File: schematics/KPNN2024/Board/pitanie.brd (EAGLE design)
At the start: 68.9 x 68.2 mm, 42 parts, among them X1 JST-2-2.5, X2 JST-2-2.5

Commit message: Платы вроде готовы
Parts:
- added 3V3, 5V: (no value), led:CHIP-LED0603
- added R11, R12: 2k, rcl:R0603
- MP1584-5V: value MP1584-B -> MP1584
- U$14: value MOLEX-4-1.25 -> BLUETOOTH
- U$9: value JST-4-2.5 -> STEP_MOT
- X1: value JST-2-2.5 -> PERE
- X2: value JST-2-2.5 -> AKKUM
- moved R8 1.90 mm to (70.7, 49.5)
- moved C1 0.10 mm to (41.4, 73.1)
- renumbered LSM to LSM6DS3, U$1 to MP1584-3V3, U$11 to LIS3MDL, U$12 to IRF7905, U$13 to DRIVER, U$4 to MP1584-5V, U$7 to 74HC595, U$8 to FOTO
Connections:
- new net N$12: 5V.A, R11.1
- new net N$13: 3V3.A, R12.1
- net 3V3: now also R12.2
- net 5V: now also R11.2
- net BUS+_OUT: now also S1.3, X2.1; no longer S1.1, X2.2
- net GND: now also 3V3.C, 5V.C, X2.2; no longer X2.1
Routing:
- net BUS+_OUT: track 20.5 -> 5.18 mm
- net N$13: track 0.00 -> 2.00 mm
- net N$12: track 0.00 -> 2.00 mm
- net OE_SR: track 49.8 -> 51.7 mm
- net 5V: track 108.6 -> 110.5 mm
- net GND: track 339.5 -> 337.8 mm
- net 3V3: track 163.4 -> 164.8 mm
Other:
- board text added: "3V3"
- board text added: "5V"
- board text added: "DIR"
- board text added: "FOTO"
- board text added: "GND"
- board text added: "LATCH"
- board text added: "MISO"
- board text added: "MOSI"
- board text added: "OE"
- board text added: "PERE"
- board text added: "RX1"
- board text added: "SCK"
- board text added: "STEP"
- board text added: "TX1"

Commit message: ййййййййййййййййййййййййййййййййййй
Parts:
- MP1584-3V3, MP1584-5V: device CanCubeSat:MP1584-B -> UNKNOWN-2024:MP1584-B
- moved MP1584-5V 14.3 mm to (59.6, 65.8)
- moved MP1584-3V3 14.2 mm to (41.2, 65.8)
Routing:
- net BUS+: track 98.8 -> 99.7 mm

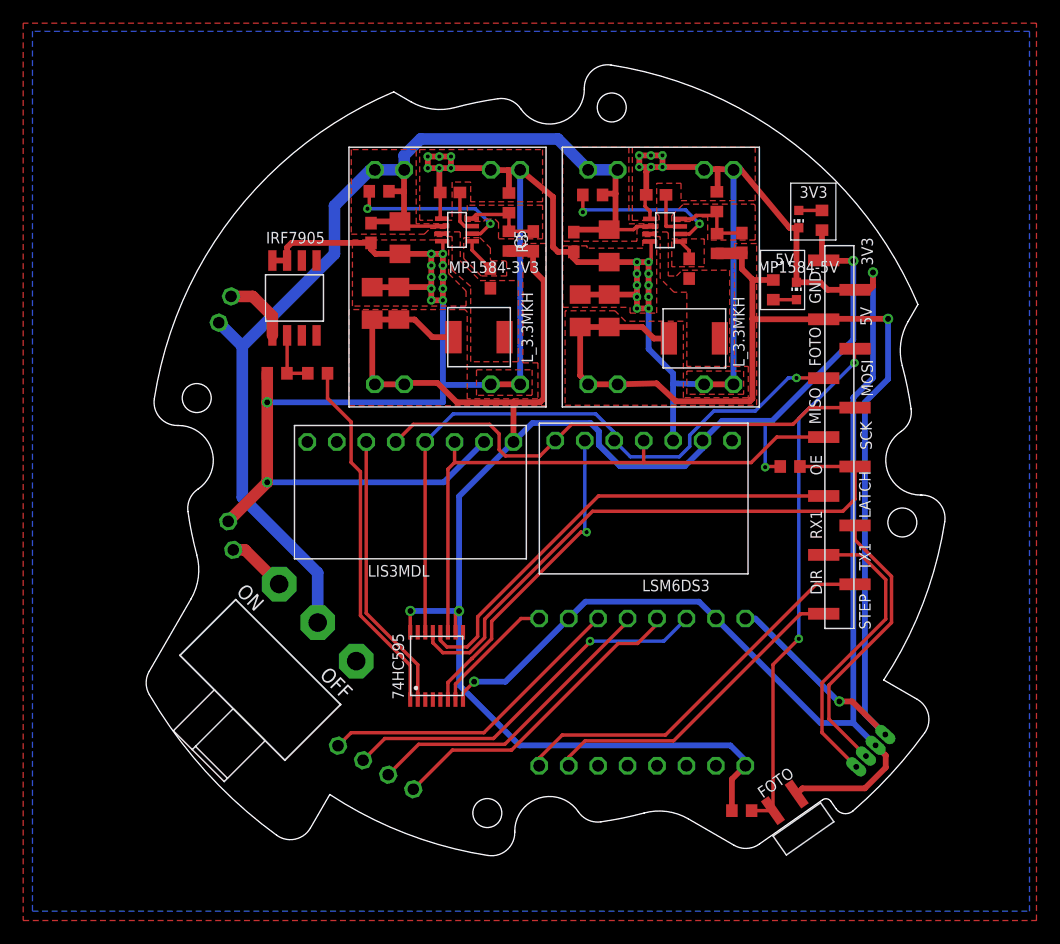
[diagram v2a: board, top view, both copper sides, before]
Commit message: поправила платы
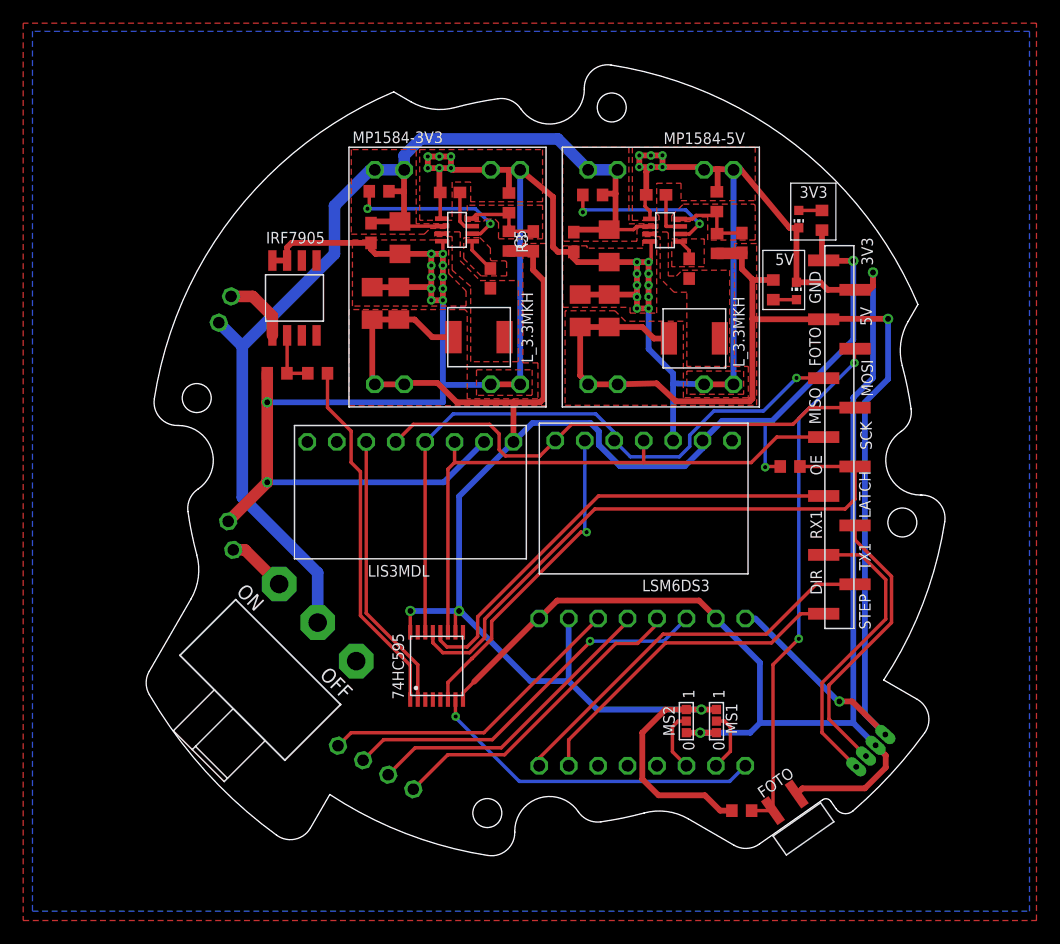
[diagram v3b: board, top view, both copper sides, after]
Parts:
- added MS1, MS2: CONNECT_3, UNKNOWN-2024:CONNECT_3
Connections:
- new net MS1: DRIVER.P$7, MS1.2
- new net MS2: DRIVER.P$6, MS2.2
- net 3V3: now also DRIVER.P10, MS1.1, MS2.1; no longer DRIVER.P$10
- net GND: now also MS1.3, MS2.3
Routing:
- net EN_DRIVER: track 10.9 -> 29.4 mm, vias 0 -> 1
- net 3V3: track 165.0 -> 176.4 mm, vias 4 -> 5
- net GND: track 338.1 -> 349.5 mm
- net MS1: track 0.00 -> 5.27 mm
- net MS2: track 0.00 -> 5.26 mm
- net STEP_DRIVER: track 27.9 -> 28.7 mm

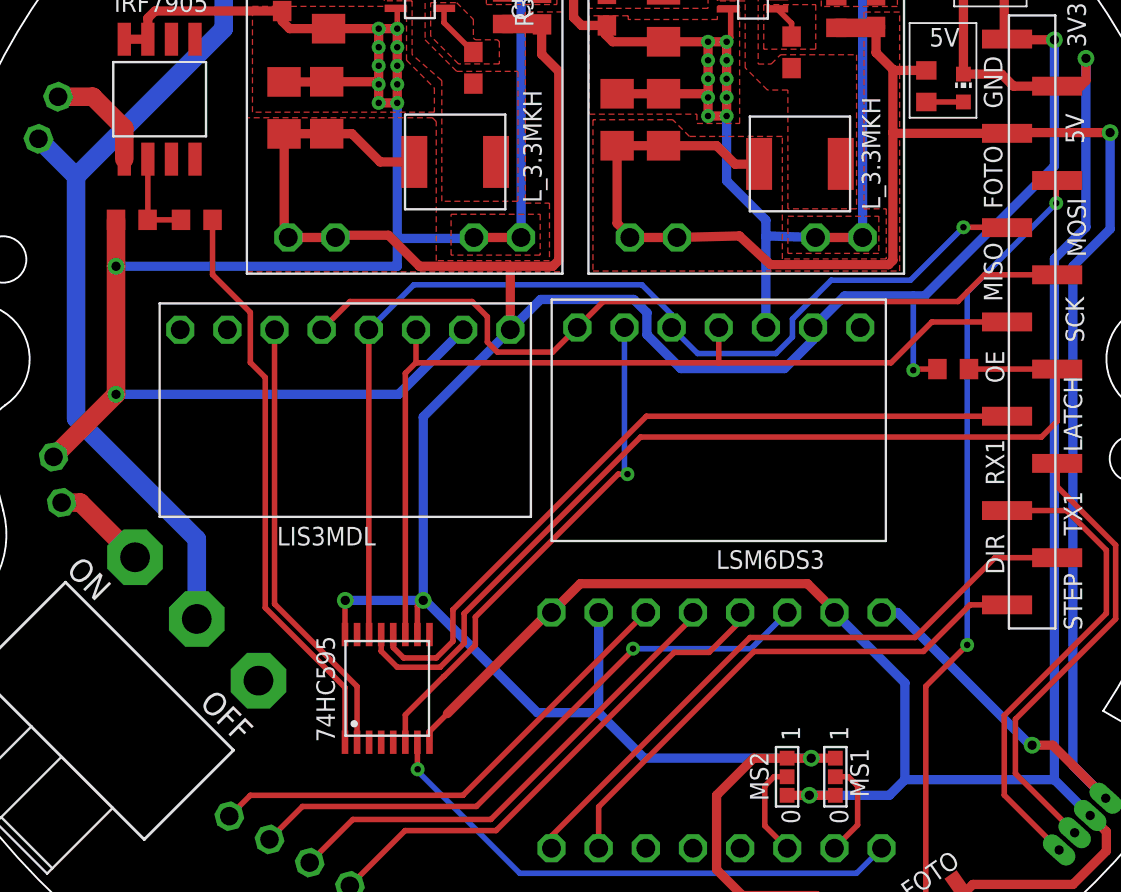
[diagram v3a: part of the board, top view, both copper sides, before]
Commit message: Модели поправлены в соответствии с платами
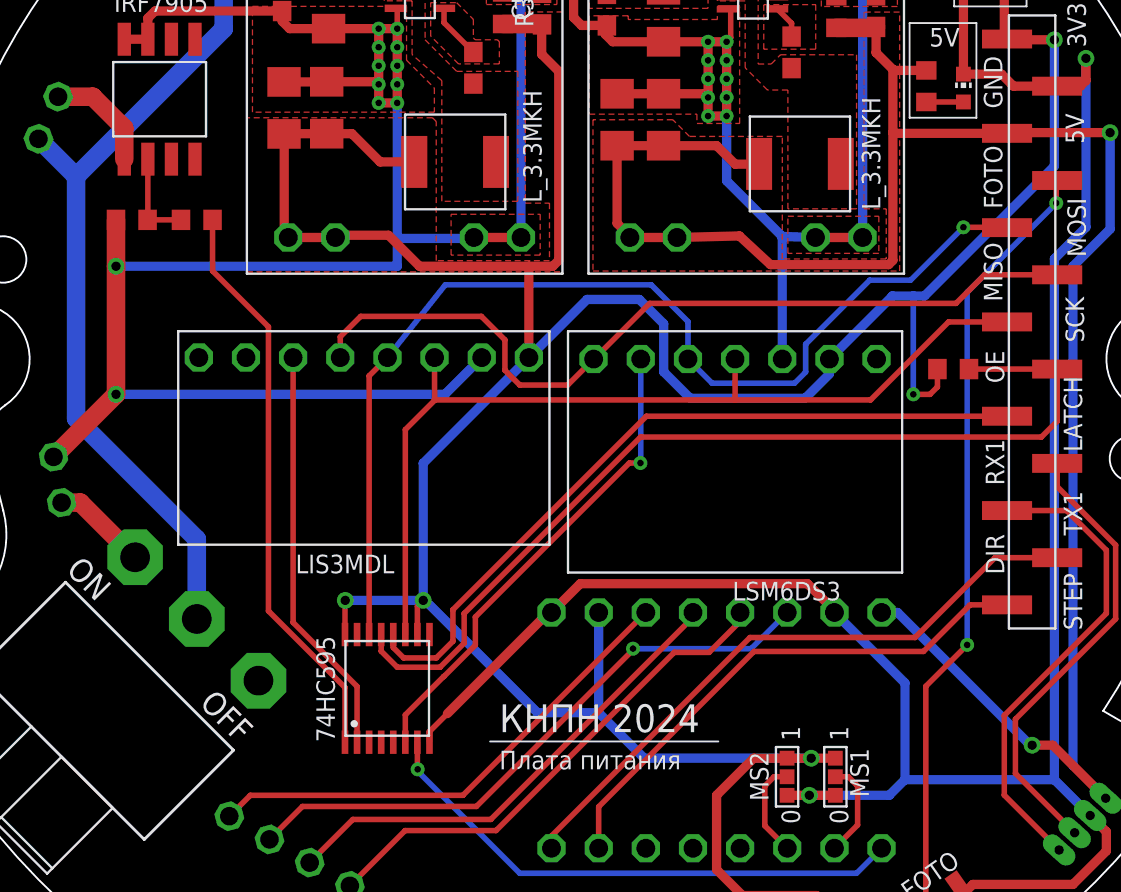
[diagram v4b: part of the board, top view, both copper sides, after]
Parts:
- added U$1: Плата питания, UNKNOWN-2024:LOGO
- R2, R5: value 8k87 -> 10k
- R3: value 40k2 -> 31k6
- R6: value 40k2 -> 53k6
- moved LSM6DS3 1.91 mm to (59.0, 45.0)
- moved LIS3MDL 1.80 mm to (39.0, 45.0)
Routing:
- net 3V3: track 176.4 -> 181.1 mm
- net CS_LIS: track 24.1 -> 22.1 mm
- net GND: track 349.5 -> 351.1 mm
- net CS_LSM: track 27.7 -> 26.3 mm
- net MISO_SR: track 43.9 -> 45.1 mm
- net MOSI_SR: track 57.1 -> 58.3 mm
- net SCK_SR: track 51.3 -> 50.3 mm
